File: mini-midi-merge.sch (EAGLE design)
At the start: 66 parts, among them IC1 PIC16F1825SO14, IC10 6N138, IC2 PIC12F1822SO08, IC3 PIC12F1822SO08, IC4 PIC12F1822SO08, IC5 REG1117, IC7 6N138, IC8 6N138, IC9 6N138, X5 DIN5PIN

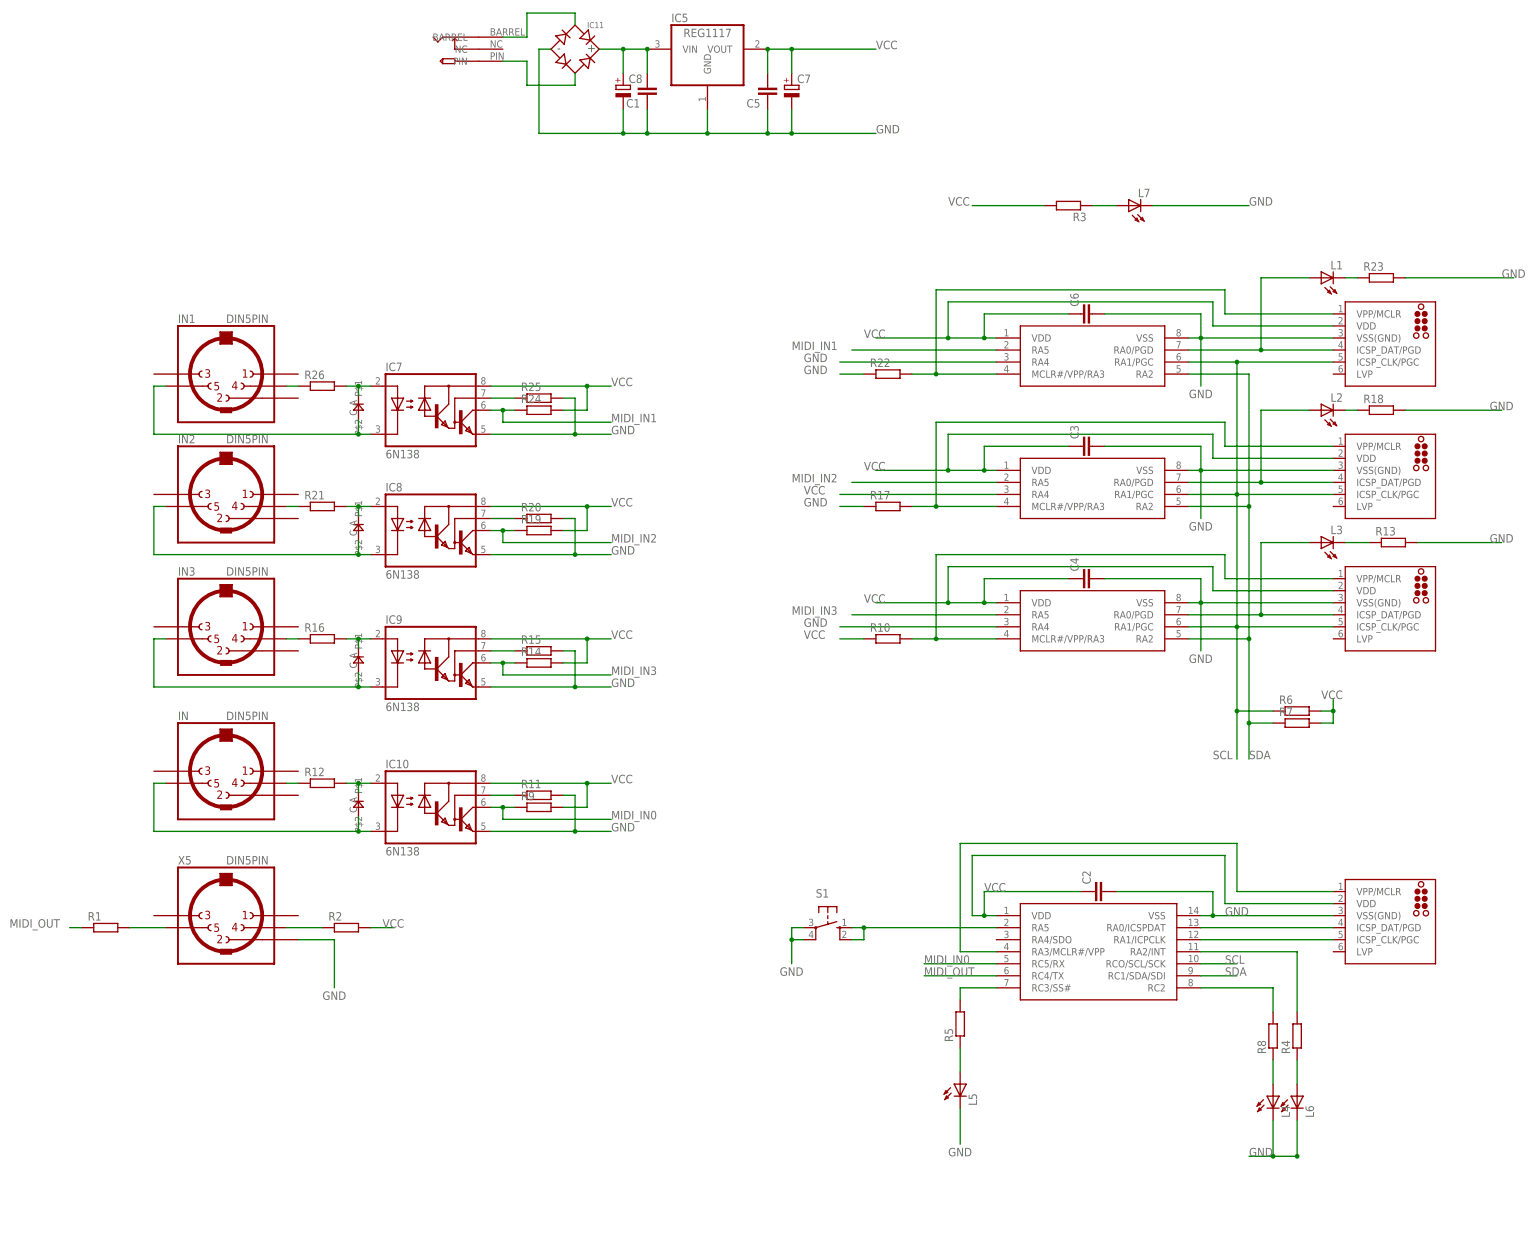
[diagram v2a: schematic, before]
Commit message: adding comp values
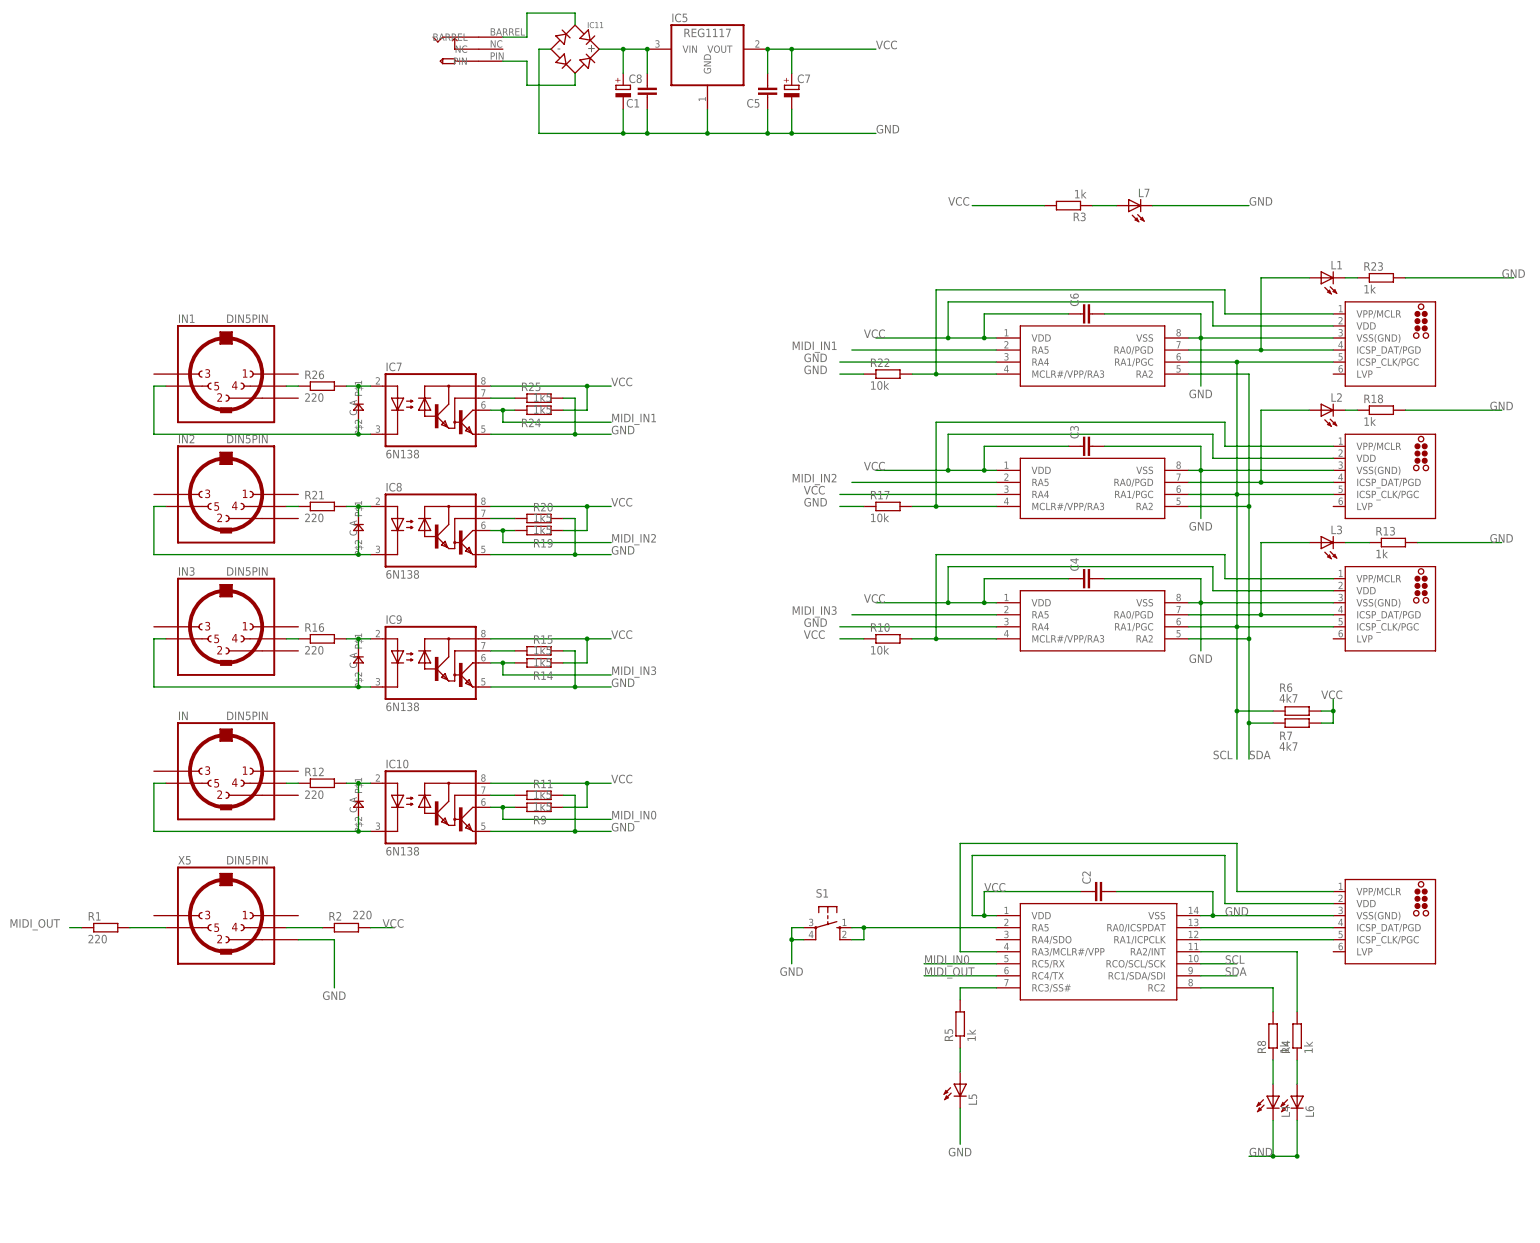
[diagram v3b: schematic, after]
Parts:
- R1, R12, R16, R2, R21, R26: value (none) -> 220
- R10, R17, R22: value (none) -> 10k
- R11, R14, R15, R19, R20, R24, R25, R9: value (none) -> 1k5
- R13, R18, R23, R3, R4, R5, R8: value (none) -> 1k
- R6, R7: value (none) -> 4k7
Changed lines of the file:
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@@
 <part name="D2" library="jasons_stuff" deviceset="0805DIODE" device=""/>
 <part name="C6" library="rcl" deviceset="C-EU" device="C0805"/>
-<part name="R16" library="rcl" deviceset="R-EU_" device="R0805"/>
-<part name="R15" library="rcl" deviceset="R-EU_" device="R0805"/>
-<part name="R14" library="rcl" deviceset="R-EU_" device="R0805"/>
+<part name="R16" library="rcl" deviceset="R-EU_" device="R0805" value="220"/>
+<part name="R15" library="rcl" deviceset="R-EU_" device="R0805" value="1k5"/>
+<part name="R14" library="rcl" deviceset="R-EU_" device="R0805" value="1k5"/>
 <part name="IN3" library="jason_eagle6" deviceset="DIN5PIN" device=""/>
 <part name="IC8" library="optocoupler" deviceset="6N138" device=""/>
 <part name="D3" library="jasons_stuff" deviceset="0805DIODE" device=""/>
-<part name="R21" library="rcl" deviceset="R-EU_" device="R0805"/>
-<part name="R20" library="rcl" deviceset="R-EU_" device="R0805"/>
-<part name="R19" library="rcl" deviceset="R-EU_" device="R0805"/>
+<part name="R21" library="rcl" deviceset="R-EU_" device="R0805" value="220"/>
+<part name="R20" library="rcl" deviceset="R-EU_" device="R0805" value="1k5"/>
+<part name="R19" library="rcl" deviceset="R-EU_" device="R0805" value="1k5"/>
 <part name="IN2" library="jason_eagle6" deviceset="DIN5PIN" device=""/>
 <part name="IC7" library="optocoupler" deviceset="6N138" device=""/>
 <part name="D4" library="jasons_stuff" deviceset="0805DIODE" device=""/>
-<part name="R26" library="rcl" deviceset="R-EU_" device="R0805"/>
-<part name="R25" library="rcl" deviceset="R-EU_" device="R0805"/>
-<part name="R24" library="rcl" deviceset="R-EU_" device="R0805"/>
+<part name="R26" library="rcl" deviceset="R-EU_" device="R0805" value="220"/>
+<part name="R25" library="rcl" deviceset="R-EU_" device="R0805" value="1k5"/>
+<part name="R24" library="rcl" deviceset="R-EU_" device="R0805" value="1k5"/>
 <part name="IN1" library="jason_eagle6" deviceset="DIN5PIN" device=""/>
 <part name="IC10" library="optocoupler" deviceset="6N138" device=""/>
 <part name="D1" library="jasons_stuff" deviceset="0805DIODE" device=""/>
-<part name="R12" library="rcl" deviceset="R-EU_" device="R0805"/>
-<part name="R11" library="rcl" deviceset="R-EU_" device="R0805"/>
-<part name="R9" library="rcl" deviceset="R-EU_" device="R0805"/>
+<part name="R12" library="rcl" deviceset="R-EU_" device="R0805" value="220"/>
+<part name="R11" library="rcl" deviceset="R-EU_" device="R0805" value="1k5"/>
+<part name="R9" library="rcl" deviceset="R-EU_" device="R0805" value="1k5"/>
 <part name="IN" library="jason_eagle6" deviceset="DIN5PIN" device=""/>
 <part name="ICSP4" library="tag-connect" deviceset="TC2030" device="-MCP-NL"/>
@@
 <part name="ICSP1" library="tag-connect" deviceset="TC2030" device="-MCP-NL"/>
 <part name="X5" library="jason_eagle6" deviceset="DIN5PIN" device=""/>
-<part name="R1" library="rcl" deviceset="R-EU_" device="R0805"/>
-<part name="R2" library="rcl" deviceset="R-EU_" device="R0805"/>
+<part name="R1" library="rcl" deviceset="R-EU_" device="R0805" value="220"/>
+<part name="R2" library="rcl" deviceset="R-EU_" device="R0805" value="220"/>
 <part name="C2" library="rcl" deviceset="C-EU" device="C0805"/>
-<part name="R6" library="rcl" deviceset="R-EU_" device="R0805"/>
-<part name="R7" library="rcl" deviceset="R-EU_" device="R0805"/>
-<part name="R8" library="rcl" deviceset="R-EU_" device="R0805"/>
-<part name="R4" library="rcl" deviceset="R-EU_" device="R0805"/>
+<part name="R6" library="rcl" deviceset="R-EU_" device="R0805" value="4k7"/>
+<part name="R7" library="rcl" deviceset="R-EU_" device="R0805" value="4k7"/>
+<part name="R8" library="rcl" deviceset="R-EU_" device="R0805" value="1k"/>
+<part name="R4" library="rcl" deviceset="R-EU_" device="R0805" value="1k"/>
 <part name="L4" library="led" deviceset="LED" device="3MM"/>
 <part name="L6" library="led" deviceset="LED" device="3MM"/>
@@
 <part name="C7" library="rcl" deviceset="CPOL-EU" device="E2,5-6E"/>
 <part name="IC11" library="microbuilder" deviceset="BRIDGERECTIFIER" device=""/>
-<part name="R3" library="rcl" deviceset="R-EU_" device="R0805"/>
+<part name="R3" library="rcl" deviceset="R-EU_" device="R0805" value="1k"/>
 <part name="L7" library="led" deviceset="LED" device="3MM"/>
-<part name="R22" library="rcl" deviceset="R-EU_" device="R0805"/>
-<part name="R17" library="rcl" deviceset="R-EU_" device="R0805"/>
-<part name="R10" library="rcl" deviceset="R-EU_" device="R0805"/>
-<part name="R23" library="rcl" deviceset="R-EU_" device="R0805"/>
+<part name="R22" library="rcl" deviceset="R-EU_" device="R0805" value="10k"/>
+<part name="R17" library="rcl" deviceset="R-EU_" device="R0805" value="10k"/>
+<part name="R10" library="rcl" deviceset="R-EU_" device="R0805" value="10k"/>
+<part name="R23" library="rcl" deviceset="R-EU_" device="R0805" value="1k"/>
 <part name="L1" library="led" deviceset="LED" device="3MM"/>
-<part name="R18" library="rcl" deviceset="R-EU_" device="R0805"/>
+<part name="R18" library="rcl" deviceset="R-EU_" device="R0805" value="1k"/>
 <part name="L2" library="led" deviceset="LED" device="3MM"/>
-<part name="R13" library="rcl" deviceset="R-EU_" device="R0805"/>
+<part name="R13" library="rcl" deviceset="R-EU_" device="R0805" value="1k"/>
 <part name="L3" library="led" deviceset="LED" device="3MM"/>
 <part name="U$9" library="jason_eagle6" deviceset="PWR_SOCKET_2_1MM" device=""/>
 <part name="S1" library="switch-omron" deviceset="10-XX" device=""/>
-<part name="R5" library="rcl" deviceset="R-EU_" device="R0805"/>
+<part name="R5" library="rcl" deviceset="R-EU_" device="R0805" value="1k"/>
 <part name="L5" library="led" deviceset="LED" device="3MM"/>
 </parts>
@@
 <instance part="C6" gate="G$1" x="157.48" y="200.66" rot="R90"/>
 <instance part="R16" gate="G$1" x="-2.54" y="132.08"/>
-<instance part="R15" gate="G$1" x="43.18" y="129.54"/>
-<instance part="R14" gate="G$1" x="43.18" y="127"/>
+<instance part="R15" gate="G$1" x="43.18" y="129.54" smashed="yes">
+<attribute name="NAME" x="41.91" y="131.0386" size="1.778" layer="95"/>
+<attribute name="VALUE" x="41.91" y="128.778" size="1.778" layer="96"/>
+</instance>
+<instance part="R14" gate="G$1" x="43.18" y="127" smashed="yes">
+<attribute name="NAME" x="41.91" y="123.4186" size="1.778" layer="95"/>
+<attribute name="VALUE" x="41.91" y="126.238" size="1.778" layer="96"/>
+</instance>
 <instance part="IN3" gate="G$1" x="-22.86" y="134.62"/>
 <instance part="IC8" gate="G$1" x="20.32" y="154.94"/>
 <instance part="D3" gate="G$1" x="5.08" y="157.48"/>
 <instance part="R21" gate="G$1" x="-2.54" y="160.02"/>
-<instance part="R20" gate="G$1" x="43.18" y="157.48"/>
-<instance part="R19" gate="G$1" x="43.18" y="154.94"/>
+<instance part="R20" gate="G$1" x="43.18" y="157.48" smashed="yes">
+<attribute name="NAME" x="41.91" y="158.9786" size="1.778" layer="95"/>
+<attribute name="VALUE" x="41.91" y="156.718" size="1.778" layer="96"/>
+</instance>
+<instance part="R19" gate="G$1" x="43.18" y="154.94" smashed="yes">
+<attribute name="NAME" x="41.91" y="151.3586" size="1.778" layer="95"/>
+<attribute name="VALUE" x="41.91" y="154.178" size="1.778" layer="96"/>
+</instance>
 <instance part="IN2" gate="G$1" x="-22.86" y="162.56"/>
 <instance part="IC7" gate="G$1" x="20.32" y="180.34"/>
 <instance part="D4" gate="G$1" x="5.08" y="182.88"/>
 <instance part="R26" gate="G$1" x="-2.54" y="185.42"/>
-<instance part="R25" gate="G$1" x="43.18" y="182.88"/>
-<instance part="R24" gate="G$1" x="43.18" y="180.34"/>
+<instance part="R25" gate="G$1" x="43.18" y="182.88" smashed="yes">
+<attribute name="NAME" x="39.37" y="184.3786" size="1.778" layer="95"/>
+<attribute name="VALUE" x="41.91" y="182.118" size="1.778" layer="96"/>
+</instance>
+<instance part="R24" gate="G$1" x="43.18" y="180.34" smashed="yes">
+<attribute name="NAME" x="39.37" y="176.7586" size="1.778" layer="95"/>
+<attribute name="VALUE" x="41.91" y="179.578" size="1.778" layer="96"/>
+</instance>
 <instance part="IN1" gate="G$1" x="-22.86" y="187.96"/>
 <instance part="IC10" gate="G$1" x="20.32" y="96.52"/>
 <instance part="D1" gate="G$1" x="5.08" y="99.06"/>
 <instance part="R12" gate="G$1" x="-2.54" y="101.6"/>
-<instance part="R11" gate="G$1" x="43.18" y="99.06"/>
-<instance part="R9" gate="G$1" x="43.18" y="96.52"/>
+<instance part="R11" gate="G$1" x="43.18" y="99.06" smashed="yes">
+<attribute name="NAME" x="41.91" y="100.5586" size="1.778" layer="95"/>
+<attribute name="VALUE" x="41.91" y="98.298" size="1.778" layer="96"/>
+</instance>
+<instance part="R9" gate="G$1" x="43.18" y="96.52" smashed="yes">
+<attribute name="NAME" x="41.91" y="92.9386" size="1.778" layer="95"/>
+<attribute name="VALUE" x="41.91" y="95.758" size="1.778" layer="96"/>
+</instance>
 <instance part="IN" gate="G$1" x="-22.86" y="104.14"/>
 <instance part="ICSP4" gate="G$1" x="223.52" y="193.04"/>
@@
 <instance part="X5" gate="G$1" x="-22.86" y="73.66"/>
 <instance part="R1" gate="G$1" x="-48.26" y="71.12"/>
-<instance part="R2" gate="G$1" x="2.54" y="71.12"/>
+<instance part="R2" gate="G$1" x="2.54" y="71.12" smashed="yes">
+<attribute name="NAME" x="-1.27" y="72.6186" size="1.778" layer="95"/>
+<attribute name="VALUE" x="3.81" y="72.898" size="1.778" layer="96"/>
+</instance>
 <instance part="C2" gate="G$1" x="160.02" y="78.74" rot="R90"/>
-<instance part="R6" gate="G$1" x="203.2" y="116.84"/>
-<instance part="R7" gate="G$1" x="203.2" y="114.3"/>
+<instance part="R6" gate="G$1" x="203.2" y="116.84" smashed="yes">
+<attribute name="NAME" x="199.39" y="120.8786" size="1.778" layer="95"/>
+<attribute name="VALUE" x="199.39" y="118.618" size="1.778" layer="96"/>
+</instance>
+<instance part="R7" gate="G$1" x="203.2" y="114.3" smashed="yes">
+<attribute name="NAME" x="199.39" y="110.7186" size="1.778" layer="95"/>
+<attribute name="VALUE" x="199.39" y="108.458" size="1.778" layer="96"/>
+</instance>
 <instance part="R8" gate="G$1" x="198.12" y="48.26" rot="R90"/>
 <instance part="R4" gate="G$1" x="203.2" y="48.26" rot="R90"/>

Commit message: tidy up schematic
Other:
- note added: "2016/hotchk155"
- note added: "ID0"
- note added: "ID1"
- note added: "ID2"
- note added: "MAIN PROCESSOR"
- note added: "MASTER MIDI IN"
- note added: "MIDI OUT"
- note added: "ORANGE SQUEEZE 4:1 MIDI MERGE"
- note added: "POWER SUPPLY"
- note added: "SLAVE IN A"
- note added: "SLAVE IN B"
- note added: "SLAVE IN C"
- note added: "Sixty Four Pixels Limited"
- note added: "UART TO I2C BRIDGE #1"
- note added: "UART TO I2C BRIDGE #2"
- note added: "UART TO I2C BRIDGE #3"
- moved on the sheet: C1, C2, C3, C4, C5, C7, C8, IC11, IC5, IC7, IN1, L2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
